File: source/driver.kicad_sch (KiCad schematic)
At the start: 55 parts, among them U2 AMS1117-3.3, U3 EG3112, U4 XL1509-5.0E1, U5 EG3112, U6 EG3112, U7 TX4130L/PW2902

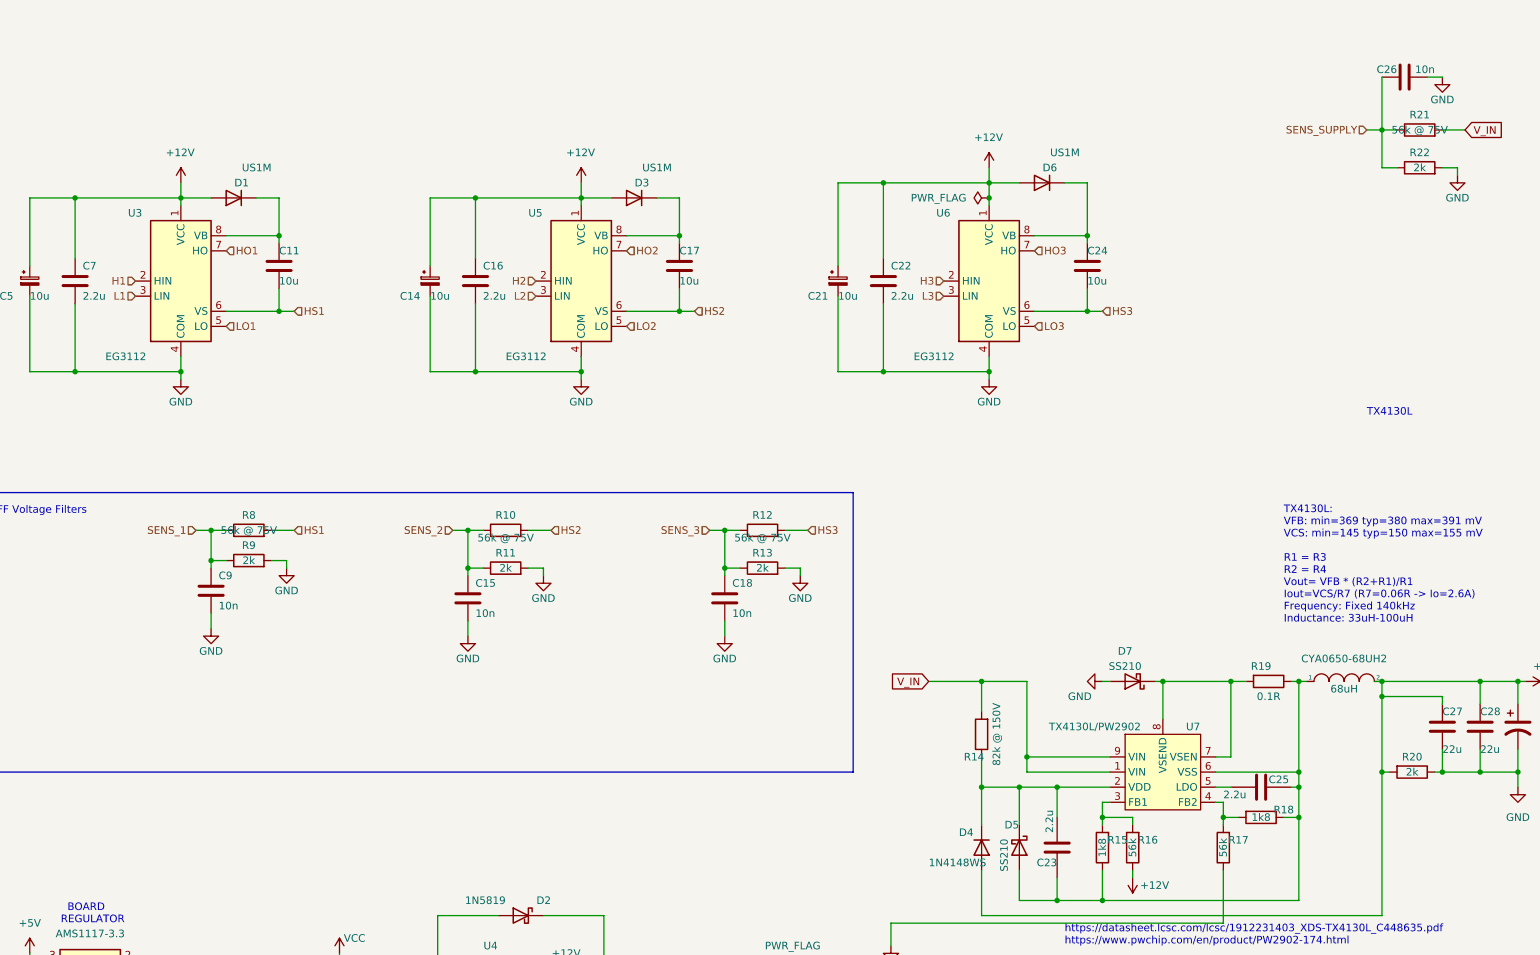
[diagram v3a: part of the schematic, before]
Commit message: 2 board setup with mcu and foc shield separated
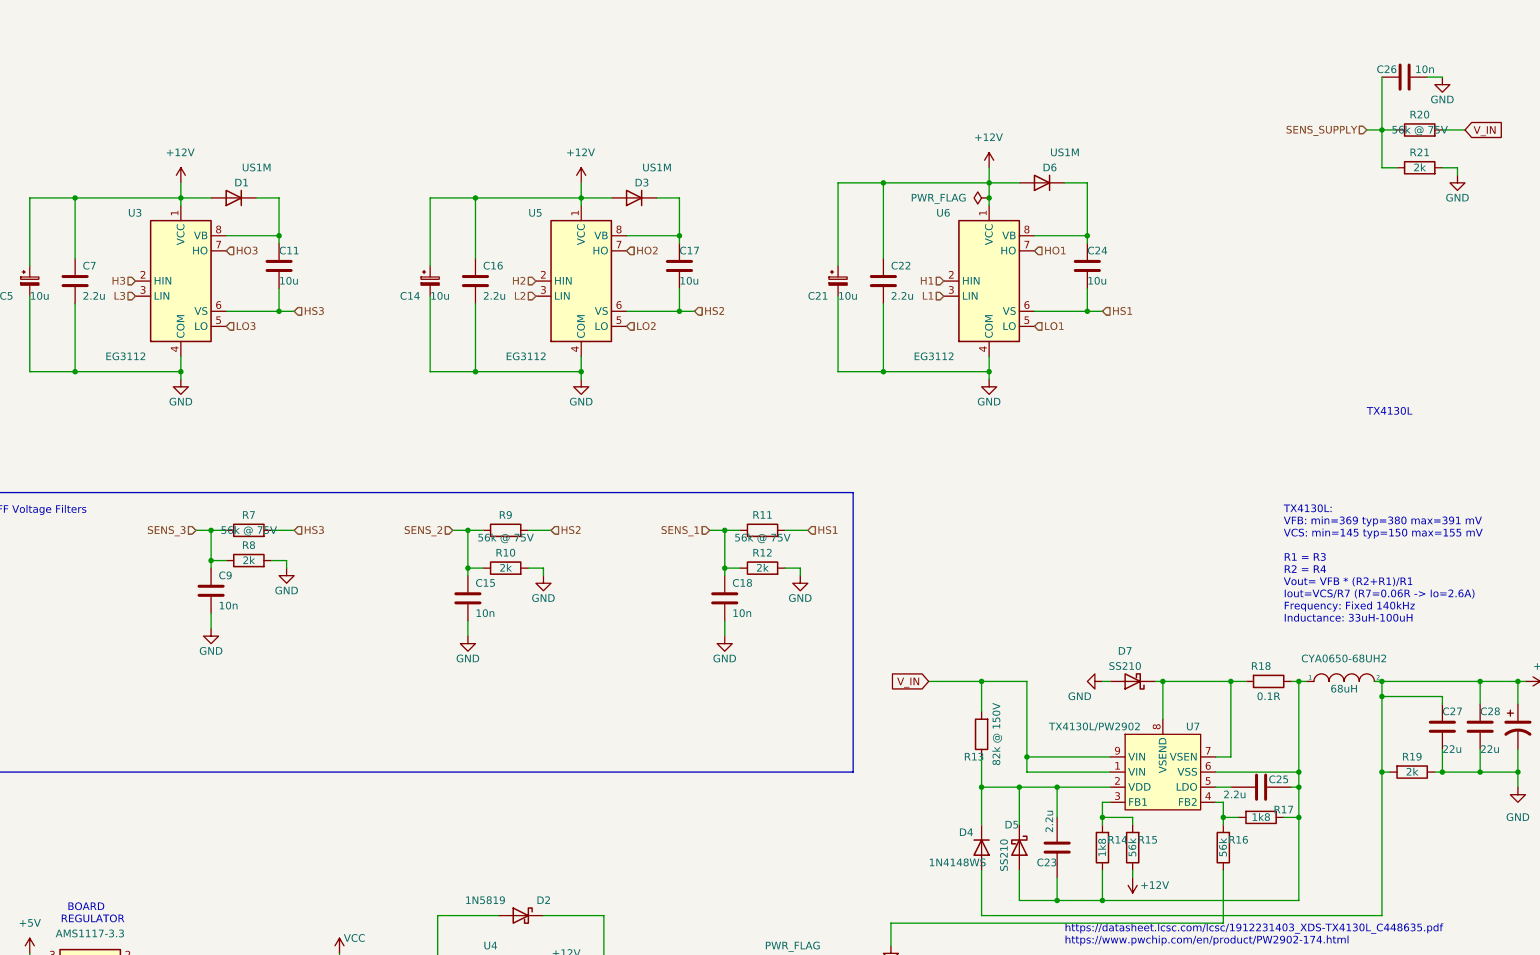
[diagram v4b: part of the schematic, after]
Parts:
- renumbered R11 to R10, R12 to R11, R13 to R12, R14 to R13, R15 to R14, R16 to R15, R17 to R16, R18 to R17, R19 to R18, R20 to R19, R21 to R20, R22 to R21, R8 to R7, R9 to R8, R10 to R9
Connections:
- net H1: now also U6.2 (HIN); no longer U3.2 (HIN)
- net H3: now also U3.2 (HIN); no longer U6.2 (HIN)
- net HO1: now also U6.7 (HO); no longer U3.7 (HO)
- net HO3: now also U3.7 (HO); no longer U6.7 (HO)
- net HS1: now also C24.2, R11.2, U6.6 (VS); no longer C11.2, R7.2, U3.6 (VS)
- net HS3: now also C11.2, R7.2, U3.6 (VS); no longer C24.2, R11.2, U6.6 (VS)
- net L1: now also U6.3 (LIN); no longer U3.3 (LIN)
- net L3: now also U3.3 (LIN); no longer U6.3 (LIN)
- net LO1: now also U6.5 (LO); no longer U3.5 (LO)
- net LO3: now also U3.5 (LO); no longer U6.5 (LO)
- net SENS_1: now also C18.1, R11.1, R12.1; no longer C9.1, R7.1, R8.1
- net SENS_3: now also C9.1, R7.1, R8.1; no longer C18.1, R11.1, R12.1

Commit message: Add files via upload
2 missing gnd connections on mcu
missing gnd connection on 12V power supply
pin4 pulled to gnd on 5V power supply
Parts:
- removed D5: SS210, Diode_SMD:D_SMA, symbol Device:D_Schottky
- added D5, D6: ZMM5V6-M zener, Diode_SMD:D_MiniMELF, symbol Diode:BZX384-xxx
- R19: value 2k -> 5.1k; LCSC C22975 -> C23186
- renumbered D6 to D7, D7 to D8
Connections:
- net +12V: no longer U4.4 (O/O)
- net GND: now also U4.4 (O/O)
- net at C23.2, D4.1 (K), R13.1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: now also D5.1 (K)
- net at C23.1, C25.1, CYA0650-68UH2.1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: now also D6.2 (A)
- new net: D5.2 (A), D6.1 (K)
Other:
- note added: "Can someone tell me, what weird feedback system this regulator uses? Attached a schematic, that is used for around 5V. Ignore the values in orange. Red are the (DC) voltages when running."
- note added: "https://www.aliexpress.com/item/33014367277.html?spm=a2g0o.productlist.0.0.46792eeeY6vAFl&algo_pvid=68456e68-51a7-4e8c-887c-c3f8ebda72ba&algo_exp_id=68456e68-51a7-4e8c-887c-c3f8ebda72ba-5&pdp_ext_f=%7B%22sku_id%22%3A%2267179048140%22%7D&pdp_npi=2%40dis%21EUR%215.11%213.32%21%21%21%21%21%40210318cf16639369713785395e9e90%2167179048140%21sea&curPageLogUid=0rY1S2RNT4Tu"
- note added: "https://www.eevblog.com/forum/projects/chinese-120v-buck-dcdc-converter-chip-search/"
- moved on the sheet: C23

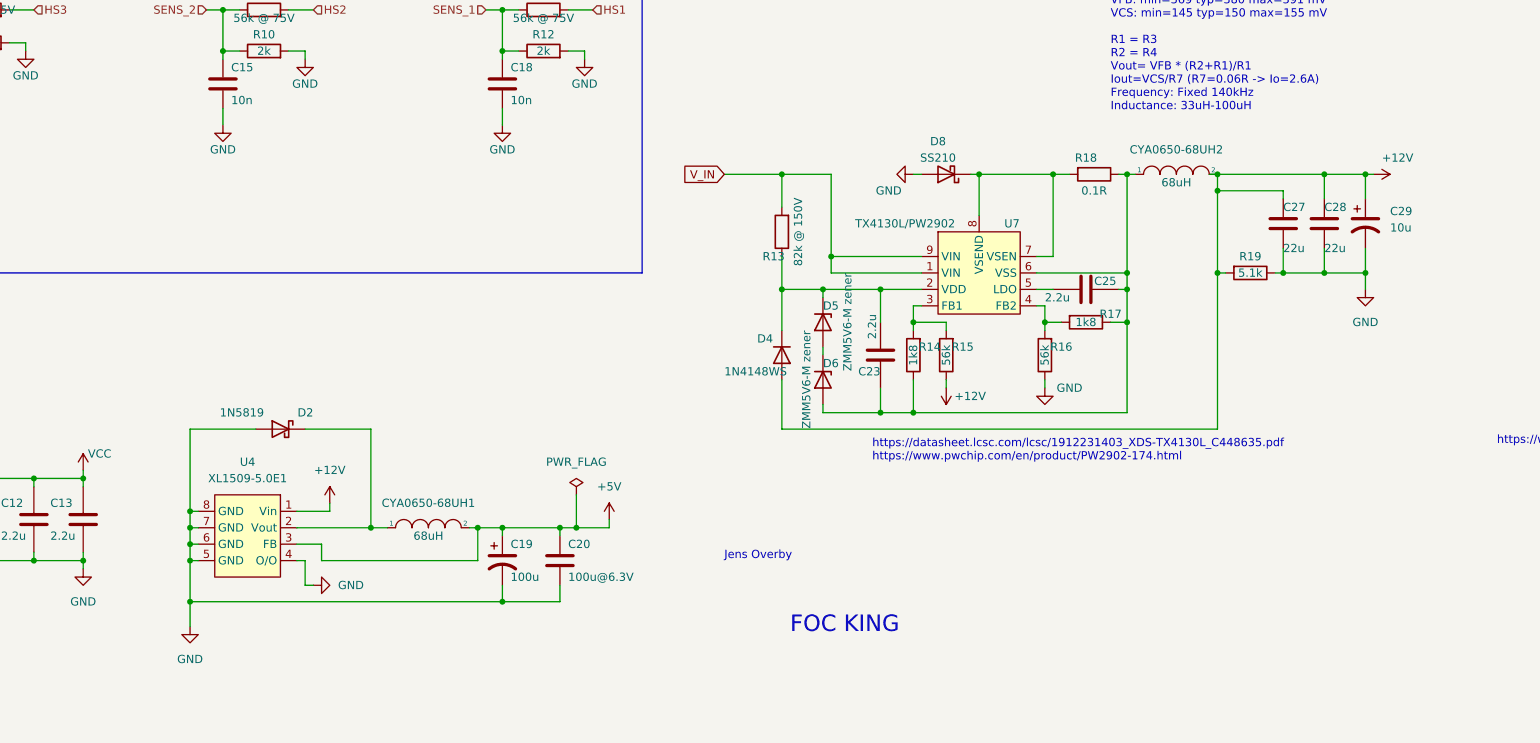
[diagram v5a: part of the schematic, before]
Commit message: JLCPCB order with separate power supply
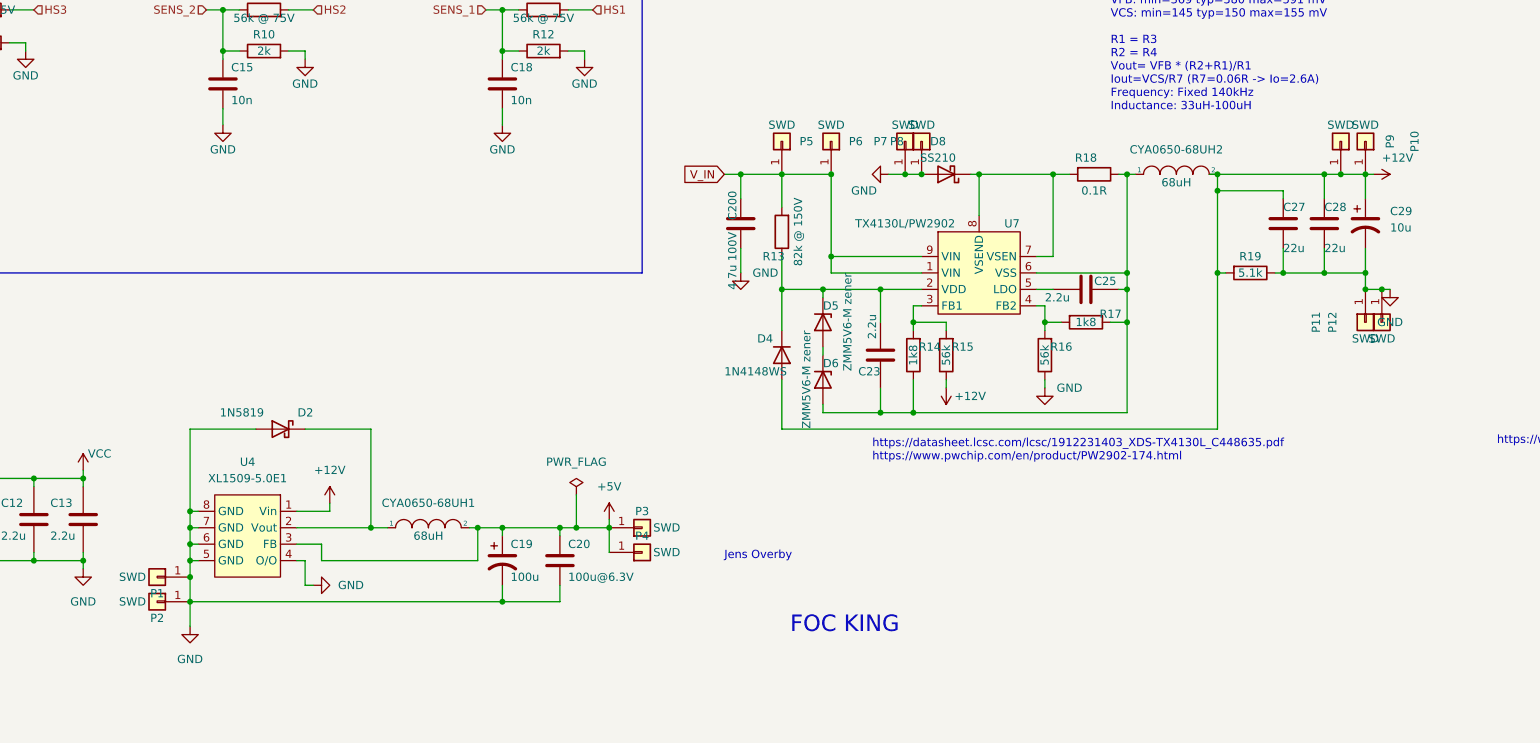
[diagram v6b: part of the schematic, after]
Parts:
- added C200: 4.7u 100V, Capacitor_SMD:C_1210_3225Metric, symbol Device:C
- added P1, P10, P11, P12, P2, P3, P4, P5, P6, P7, P8, P9: SWD, Connector_PinHeader_2.54mm:PinHeader_1x01_P2.54mm_Vertical, symbol Connector_Generic:Conn_01x01
- D5, D6: LCSC C263146 -> C8062
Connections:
- net +12V: now also P10.1 (Pin_1), P9.1 (Pin_1)
- net +5V: now also P3.1 (Pin_1), P4.1 (Pin_1)
- net GND: now also C200.1, P1.1 (Pin_1), P11.1 (Pin_1), P12.1 (Pin_1), P2.1 (Pin_1), P7.1 (Pin_1), P8.1 (Pin_1)
- net V_IN: now also C200.2, P5.1 (Pin_1), P6.1 (Pin_1)

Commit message: jlcpcb order
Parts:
- C25: renamed from C200; LCSC (none) -> C381466; LRSC C381466 -> (none)
- D2: LCSC (none) -> C191023
- renumbered C8 to C10, C9 to C11, C10 to C12, C11 to C13, C12 to C14, C13 to C15, C14 to C16, C15 to C17, C16 to C18, C17 to C19, C18 to C20, C19 to C21, C20 to C22, C21 to C23, C22 to C24, C23 to C26, C24 to C27, C25 to C28, C26 to C29, C27 to C30, C28 to C31, C29 to C32, C5 to C7, C6 to C8, C7 to C9, R8 to R10, R9 to R11, R10 to R12, R11 to R13, R12 to R14, R13 to R15, R14 to R16, R15 to R17, R16 to R18, R17 to R19, R18 to R20, R19 to R21, R20 to R22, R21 to R23, R7 to R9, U2 to U3, U3 to U4, U4 to U5, U5 to U6, U6 to U7, U7 to U8

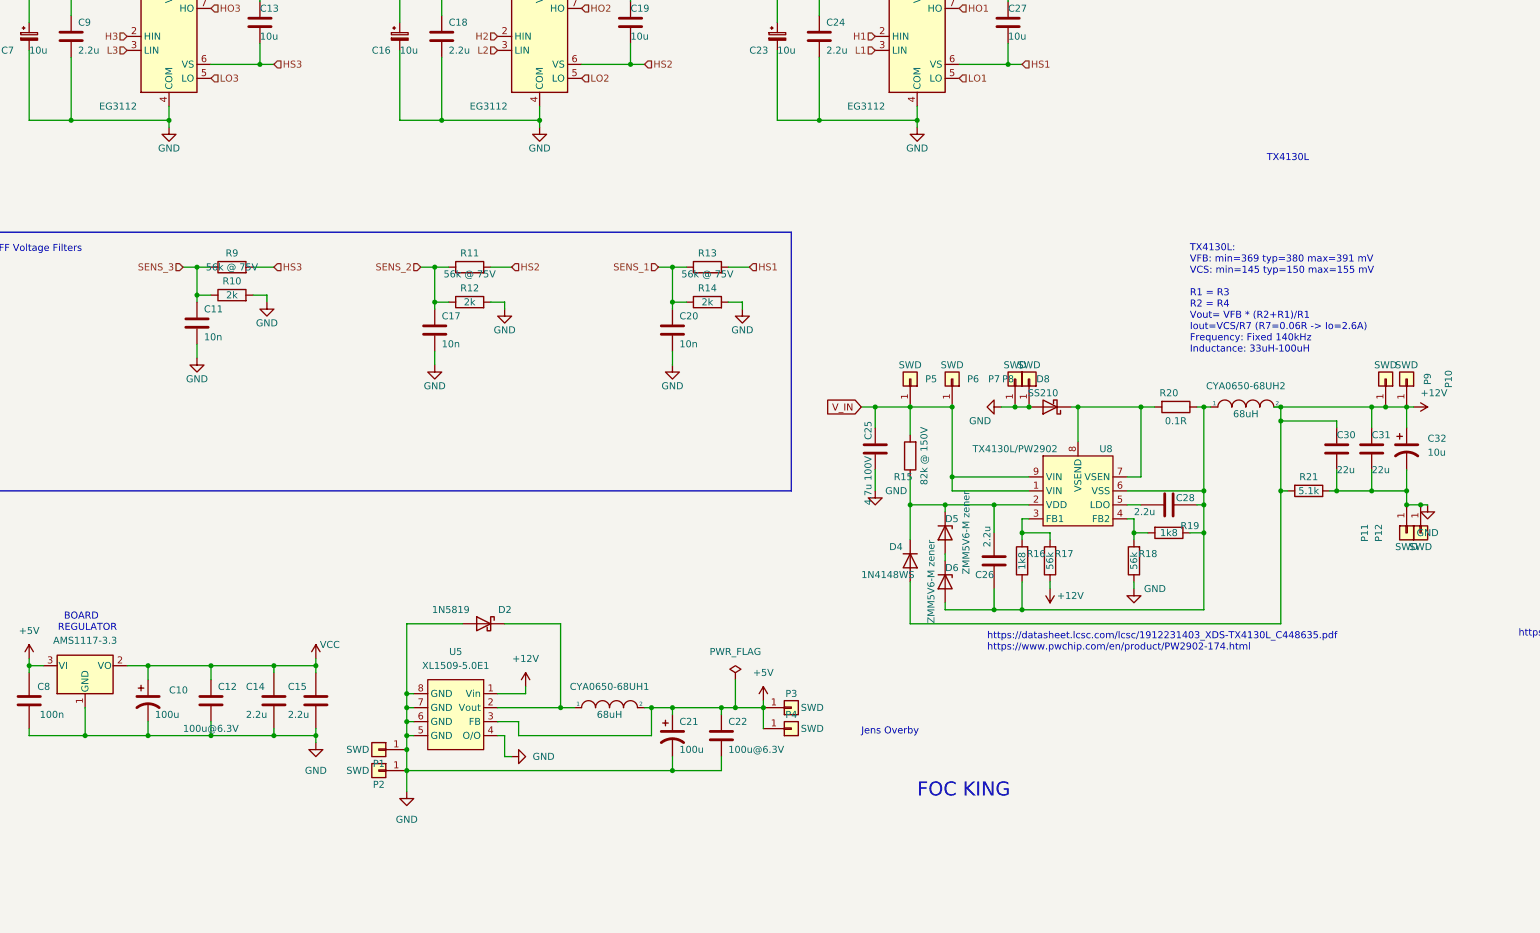
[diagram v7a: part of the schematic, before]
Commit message: jlcpcb reorder of main-module only
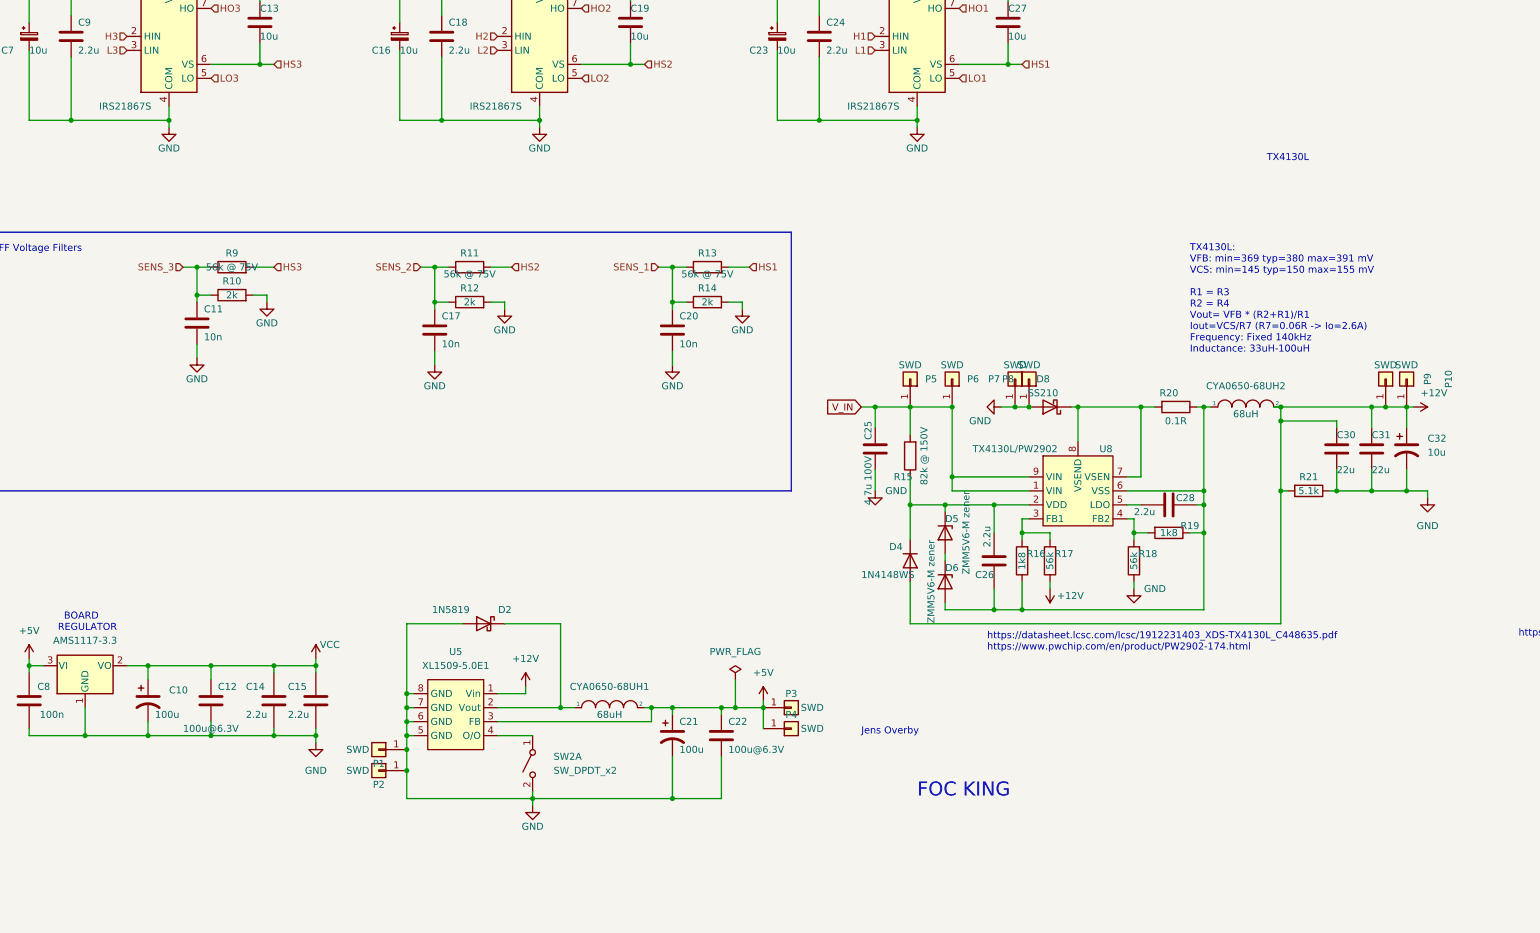
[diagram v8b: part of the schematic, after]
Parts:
- removed P11, P12: SWD, Connector_PinHeader_2.54mm:PinHeader_1x01_P2.54mm_Vertical, symbol Connector_Generic:Conn_01x01
- added SW2: SW_DPDT_x2, Jumper:SolderJumper-2_P1.3mm_Bridged_Pad1.0x1.5mm, symbol Switch:SW_DPST_x2
- U4, U6, U7: value EG3112 -> IRS21867S; LCSC C111908 -> C52290
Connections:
- net GND: now also SW2.2 (B); no longer U5.4 (O/O)
- new net: SW2.1 (A), U5.4 (O/O)
